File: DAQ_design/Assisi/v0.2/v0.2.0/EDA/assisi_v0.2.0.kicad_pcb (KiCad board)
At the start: 2 copper layers, 117 x 56 mm, 16 parts, among them Q1 BC549, Q2 IRF9540N, Q3 IRF540N, Q4 BC549, Q5 IRF540N, Q6 IRF9540N

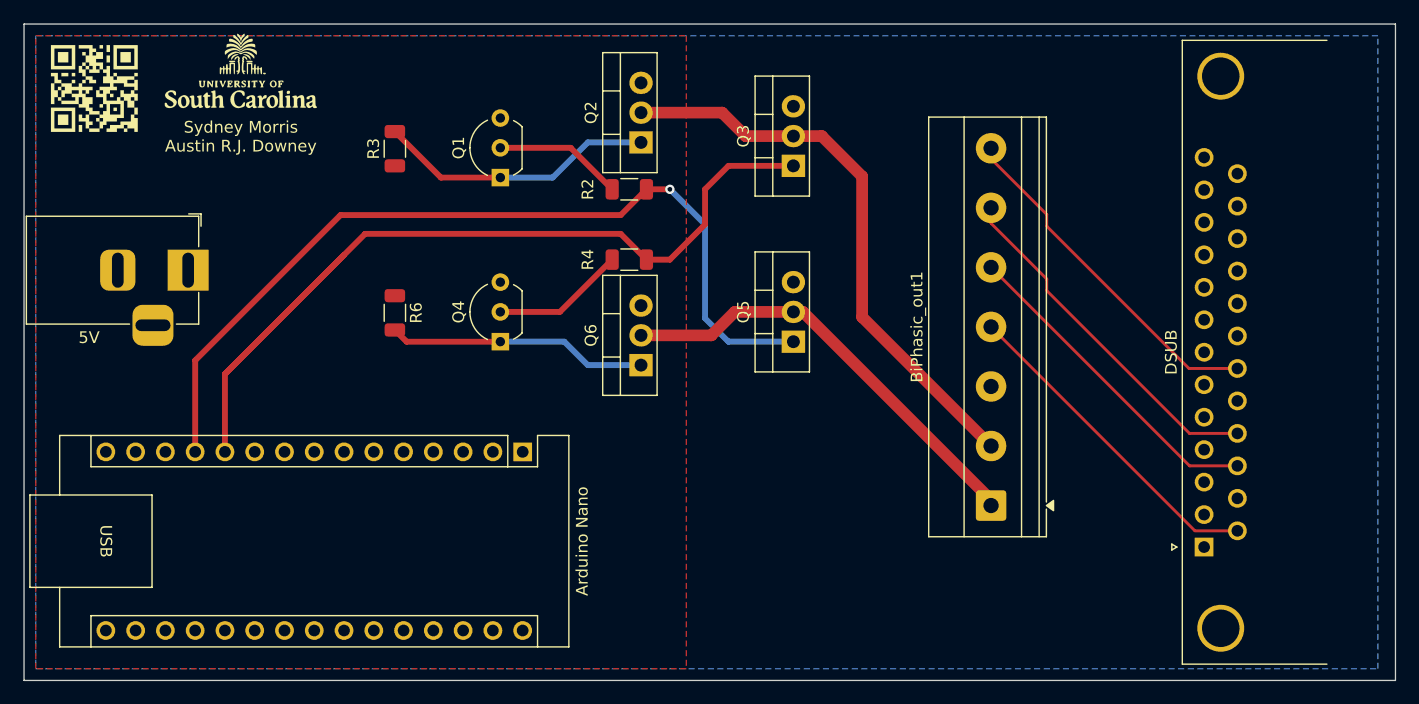
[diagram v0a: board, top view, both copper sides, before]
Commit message: rearranged pcb components
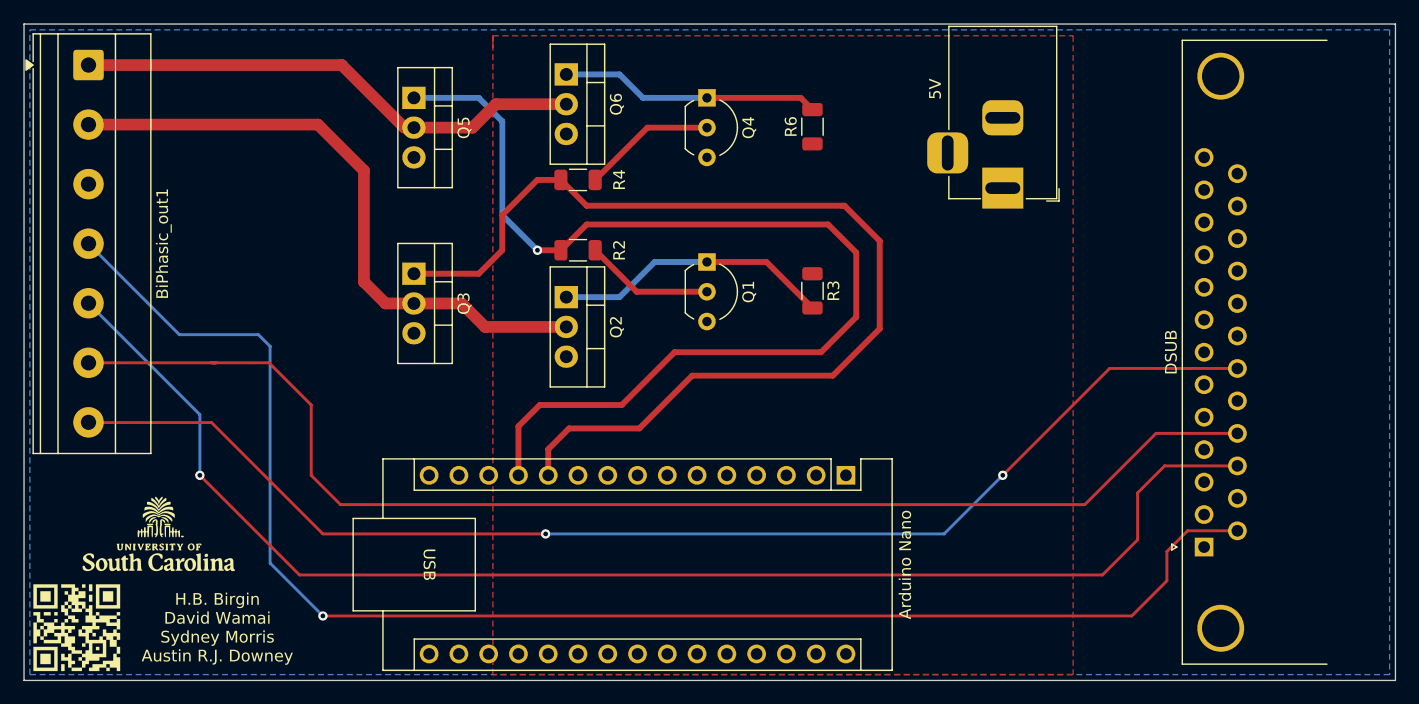
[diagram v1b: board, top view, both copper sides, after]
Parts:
- moved BiPhasic_out1 85.7 mm to (126.5, 52.5), turned to -90 degrees
- moved 5V 69.9 mm to (204.5, 63.0), turned to -90 degrees
- moved G7 46.0 mm to (125.5, 100.5)
- moved G2 40.1 mm to (132.5, 92.5)
- moved R6 39.0 mm to (188.3, 57.8), turned to 90 degrees
- moved Q5 38.5 mm to (154.3, 55.3), turned to -90 degrees
- moved R3 37.6 mm to (188.3, 71.8), turned to -90 degrees
- moved Q3 33.7 mm to (154.3, 70.3), turned to -90 degrees
- moved Arduino Nano 27.7 mm to (191.1, 87.5)
- moved Q4 27.3 mm to (179.3, 55.3), turned to -90 degrees
- moved Q6 25.6 mm to (167.3, 53.3), turned to -90 degrees
- moved Q1 19.0 mm to (179.3, 69.3), turned to -90 degrees
- moved Q2 14.7 mm to (167.3, 72.3), turned to -90 degrees
- moved R4 8.09 mm to (168.3, 62.3), turned to 180 degrees
- moved R2 6.80 mm to (168.3, 68.3), turned to 180 degrees
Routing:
- net AIN0: track 28.2 -> 126.5 mm, vias 0 -> 1
- net AIN1: track 28.0 -> 116.8 mm, vias 0 -> 1
- net AIN2: track 30.3 -> 109.9 mm
- net AIN3: track 29.9 -> 107.9 mm, vias 0 -> 2
- net LOGIC1: track 75.5 -> 92.6 mm
- net LOGIC2: track 80.4 -> 89.2 mm
- net SN: track 37.8 -> 43.8 mm
- net SP: track 48.7 -> 53.5 mm
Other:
- board text added: "H.B. Birgin David Wamai Sydney Morris Austin R.J. Downey"
- board text removed: "Sydney Morris Austin R.J. Downey"

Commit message: added title and cut pcb
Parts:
- moved G2 3.04 mm to (132.0, 89.5)
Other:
- board size 117 x 56 mm -> 111.5 x 56 mm
- board text added: "Assisi V0.2.0 05/03/2026"
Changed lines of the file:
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@@
 	(footprint "uofsc_foots:uofsc"
 		(layer "F.Cu")
-		(at 132.5 92.5)
+		(at 132 89.5)
 		(property "Reference" "G2"
 			(at 0 0 0)
@@
 	)
 	(gr_line
-		(start 238 105)
-		(end 238 49)
+		(start 232.5 105)
+		(end 232.5 49)
 		(stroke
 			(width 0.1)
@@
 	(gr_line
 		(start 121 105)
-		(end 238 105)
+		(end 232.5 105)
 		(stroke
 			(width 0.1)
@@
 	)
 	(gr_line
-		(start 238 49)
+		(start 232.5 49)
 		(end 121 49)
 		(stroke
@@
 		(layer "Edge.Cuts")
 	)
+	(gr_text "Assisi V0.2.0\n05/03/2026"
+		(at 132 96 0)
+		(layer "F.SilkS")
+		(effects
+			(font
+				(size 1 1)
+				(thickness 0.1)
+			)
+			(justify bottom)
+		)
+	)
 	(gr_text "H.B. Birgin\nDavid Wamai\nSydney Morris\nAustin R.J. Downey"
 		(at 137.5 103.5 0)
@@
 		(polygon
 			(pts
-				(xy 121.5 49.5) (xy 237.5 49.5) (xy 237.5 104.5) (xy 121.5 104.5)
+				(xy 121.5 49.5) (xy 232 49.5) (xy 232 104.5) (xy 121.5 104.5)
 			)
 		)
